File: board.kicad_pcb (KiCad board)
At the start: 2 copper layers, 85.3 x 35.3 mm, 32 parts, among them J0 Battery Pads, J1 Shard, J2 USB-Micro, SW0 RESET, SW1 UP, SW2 DOWN, SW3 LEFT, SW4 RIGHT, SW5 BTN_A, SW6 BTN_B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

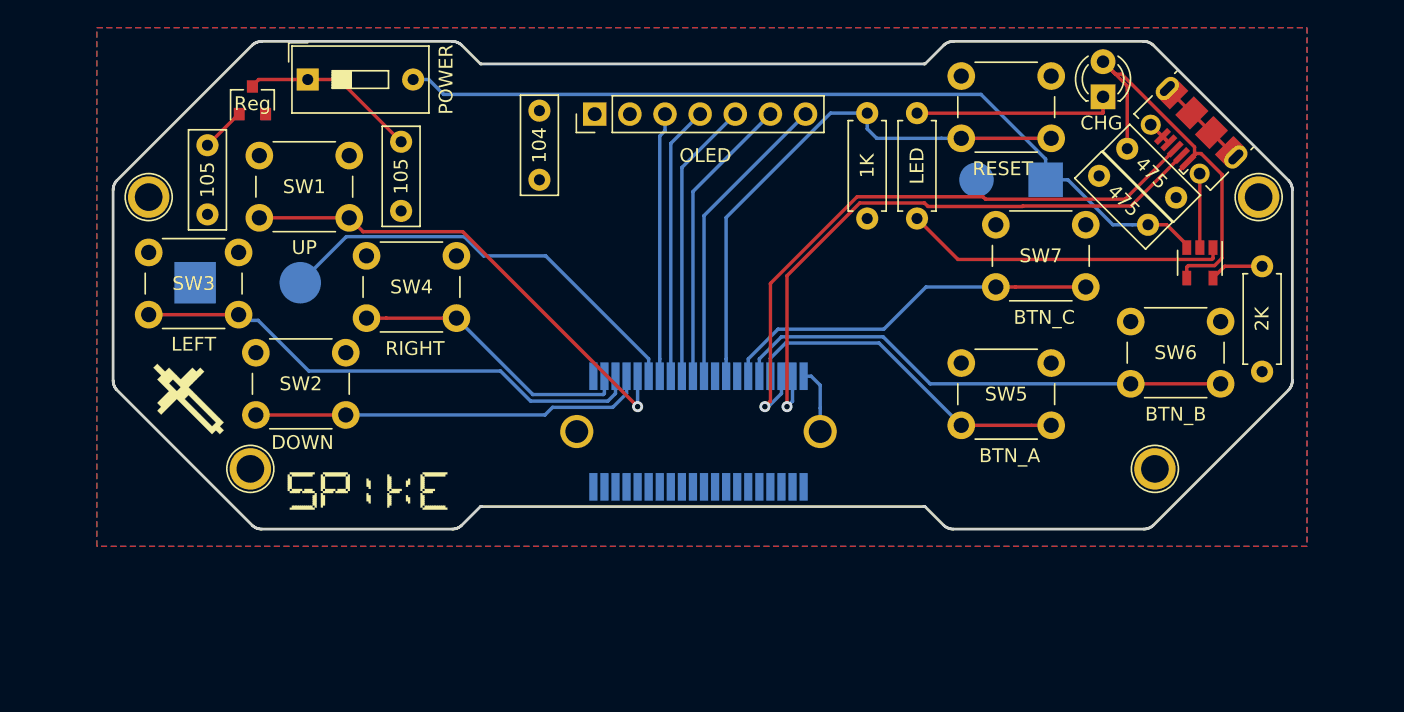
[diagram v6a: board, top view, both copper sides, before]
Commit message: changed 3.3v track to via instead of mounting point
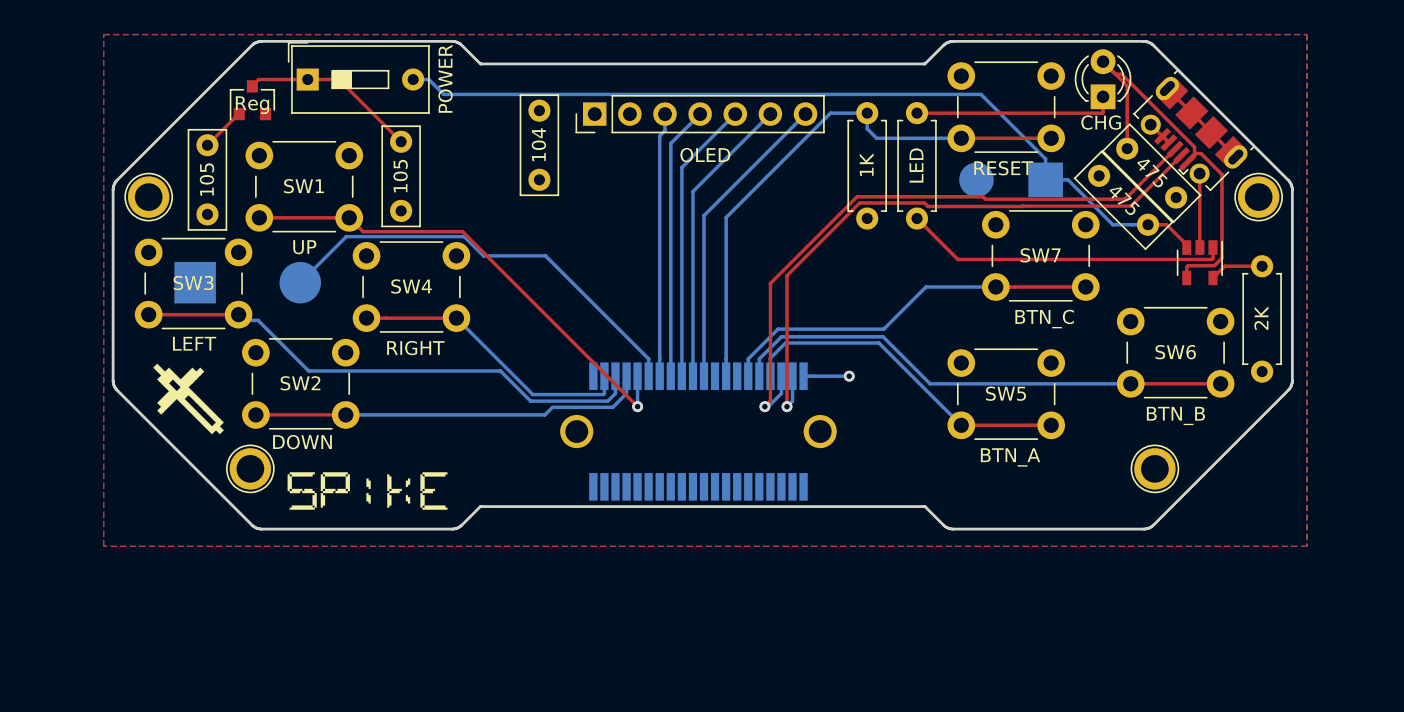
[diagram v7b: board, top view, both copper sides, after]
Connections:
- J1 pad : +3V3 -> (no net)
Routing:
- net +3V3: track 5.25 -> 3.35 mm, vias 0 -> 1
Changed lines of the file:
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@@
-(kicad_pcb (version 20171130) (host pcbnew "(5.0.1-3-g963ef8bb5)")
+(kicad_pcb (version 20171130) (host pcbnew "(5.0.0)")
   (general
     (thickness 1.6)
     (drawings 171)
-    (tracks 161)
+    (tracks 160)
     (zones 0)
     (modules 32)
@@
       (drillshape 0)
       (scaleselection 1)
-      (outputdirectory "/Users/mikewatts/Desktop/spike_gerbers/"))
+      (outputdirectory "C:/Scratch/Spike_Gerbers/"))
   )
   (net 0 "")
@@
     (pad 40 smd rect (at 15.2 4 180) (size 0.6 2) (layers B.Cu B.Paste B.Mask)
       (net 2 GND))
-    (pad "" thru_hole circle (at -1.2 0 180) (size 2.4 2.4) (drill 1.65) (layers *.Cu *.Mask)
-      (net 1 +3V3))
+    (pad "" thru_hole circle (at -1.2 0 180) (size 2.4 2.4) (drill 1.65) (layers *.Cu *.Mask))
     (pad "" thru_hole circle (at 16.4 0 180) (size 2.4 2.4) (drill 1.65) (layers *.Cu *.Mask))
   )
@@
   (gr_line (start 168.75 83.75) (end 167.3735 85.1265) (layer Edge.Cuts) (width 0.2))
   (segment (start 119.7 88.8) (end 119.7 88.75) (width 0.25) (layer F.Cu) (net 1))
-  (segment (start 159.505 111.75) (end 159.505 112.095) (width 0.25) (layer B.Cu) (net 1))
-  (segment (start 160.8 112.12) (end 160.775 112.095) (width 0.25) (layer B.Cu) (net 1))
-  (segment (start 159.8 110.002944) (end 159.8 111.7) (width 0.25) (layer B.Cu) (net 1))
-  (segment (start 159.8 108.35) (end 159.8 110.002944) (width 0.25) (layer B.Cu) (net 1))
-  (segment (start 159.15 107.7) (end 159.8 108.35) (width 0.25) (layer B.Cu) (net 1))
+  (segment (start 159.505 111.75) (end 159.505 112.095) (width 0.25) (layer B.Cu) (net 0))
+  (segment (start 160.8 112.12) (end 160.775 112.095) (width 0.25) (layer B.Cu) (net 0))
+  (via (at 161.9 107.7) (size 0.8) (drill 0.4) (layers F.Cu B.Cu) (net 1))
+  (segment (start 159.15 107.7) (end 161.9 107.7) (width 0.25) (layer B.Cu) (net 1))
   (segment (start 158.6 107.7) (end 159.15 107.7) (width 0.25) (layer B.Cu) (net 1))
   (segment (start 187.25 93.068288) (end 187.233623 93.051911) (width 0.25) (layer F.Cu) (net 2))
@@
   (segment (start 189.05 99.75) (end 188.2 100.6) (width 0.25) (layer F.Cu) (net 24))
   (segment (start 191.75 99.75) (end 189.05 99.75) (width 0.25) (layer F.Cu) (net 24))
+  (zone (net 2) (net_name GND) (layer B.Cu) (hatch edge 0.508)
+    (connect_pads (clearance 0.508))
+    (min_thickness 0.254)
+    (fill yes (arc_segments 16) (thermal_gap 0.508) (thermal_bridge_width 0.508))
+    (polygon
+      (pts
+        (xy 108 83) (xy 195 83) (xy 195 120) (xy 108 120)
+      )
+    )
+  )
   (zone (net 1) (net_name +3V3) (layer F.Cu) (hatch edge 0.508)
     (connect_pads (clearance 0.508))
@@
     (polygon
       (pts
-        (xy 107.5 82.5) (xy 195 82.5) (xy 195 120) (xy 107.5 120)
+        (xy 108 83) (xy 195 83) (xy 195 120) (xy 108 120)
       )
     )
-  )
-  (zone (net 2) (net_name GND) (layer B.Cu) (hatch edge 0.508)
-    (connect_pads (clearance 0.508))
-    (min_thickness 0.254)
-    (fill yes (arc_segments 16) (thermal_gap 0.508) (thermal_bridge_width 0.508))
-    (polygon
-      (pts
-        (xy 107.5 82.5) (xy 195 82.5) (xy 195 120) (xy 107.5 120)
-      )
-    )

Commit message: label tweaks
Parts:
- J0: value Battery Pads -> Battery
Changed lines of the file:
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@@
     (thickness 1.6)
     (drawings 171)
-    (tracks 160)
+    (tracks 158)
     (zones 0)
     (modules 32)
@@
   (page A4)
   (layers
-    (0 F.Cu signal)
+    (0 F.Cu signal hide)
     (31 B.Cu signal)
     (32 B.Adhes user hide)
@@
       (effects (font (size 1 1) (thickness 0.15)) (justify mirror))
     )
-    (fp_text value Speaker (at 4.000001 -4.5) (layer B.SilkS)
+    (fp_text value Speaker (at 3.69 6.96) (layer B.SilkS)
       (effects (font (size 1 1) (thickness 0.15)) (justify mirror))
     )
@@
       (effects (font (size 1 1) (thickness 0.15)) (justify mirror))
     )
-    (fp_text value "Battery Pads" (at 0 -2.25 180) (layer B.SilkS)
+    (fp_text value Battery (at 7.3 0 180) (layer B.SilkS)
       (effects (font (size 1 1) (thickness 0.15)) (justify mirror))
     )
@@
   (module "Custom Footprints:Samtec_MEC8-120-02-L-D-RA1_Socket" (layer B.Cu)
     (at 158.6 111.7 180)
-    (fp_text reference J1 (at 15 -2 180) (layer B.SilkS)
+    (fp_text reference J1 (at 15 -2 180) (layer B.Fab)
       (effects (font (size 1 1) (thickness 0.15)) (justify mirror))
     )
@@
   (gr_line (start 168.75 83.75) (end 167.3735 85.1265) (layer Edge.Cuts) (width 0.2))
   (segment (start 119.7 88.8) (end 119.7 88.75) (width 0.25) (layer F.Cu) (net 1))
-  (segment (start 159.505 111.75) (end 159.505 112.095) (width 0.25) (layer B.Cu) (net 0))
-  (segment (start 160.8 112.12) (end 160.775 112.095) (width 0.25) (layer B.Cu) (net 0))
   (via (at 161.9 107.7) (size 0.8) (drill 0.4) (layers F.Cu B.Cu) (net 1))
   (segment (start 159.15 107.7) (end 161.9 107.7) (width 0.25) (layer B.Cu) (net 1))
